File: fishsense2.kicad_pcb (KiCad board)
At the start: 2 copper layers, 71.1 x 73.7 mm, 20 parts, among them J1 Conn_02x10_Odd_Even, J2 Screw_Terminal_01x02, J3 Conn_01x02, J4 Conn_01x02, J5 Conn_01x02, J6 USB_C_Receptacle, J7 USB_C_Receptacle, J8 USB_C_Receptacle, K1 ADW11, U1 P783F-Q24-S5-S, U2 AD9951

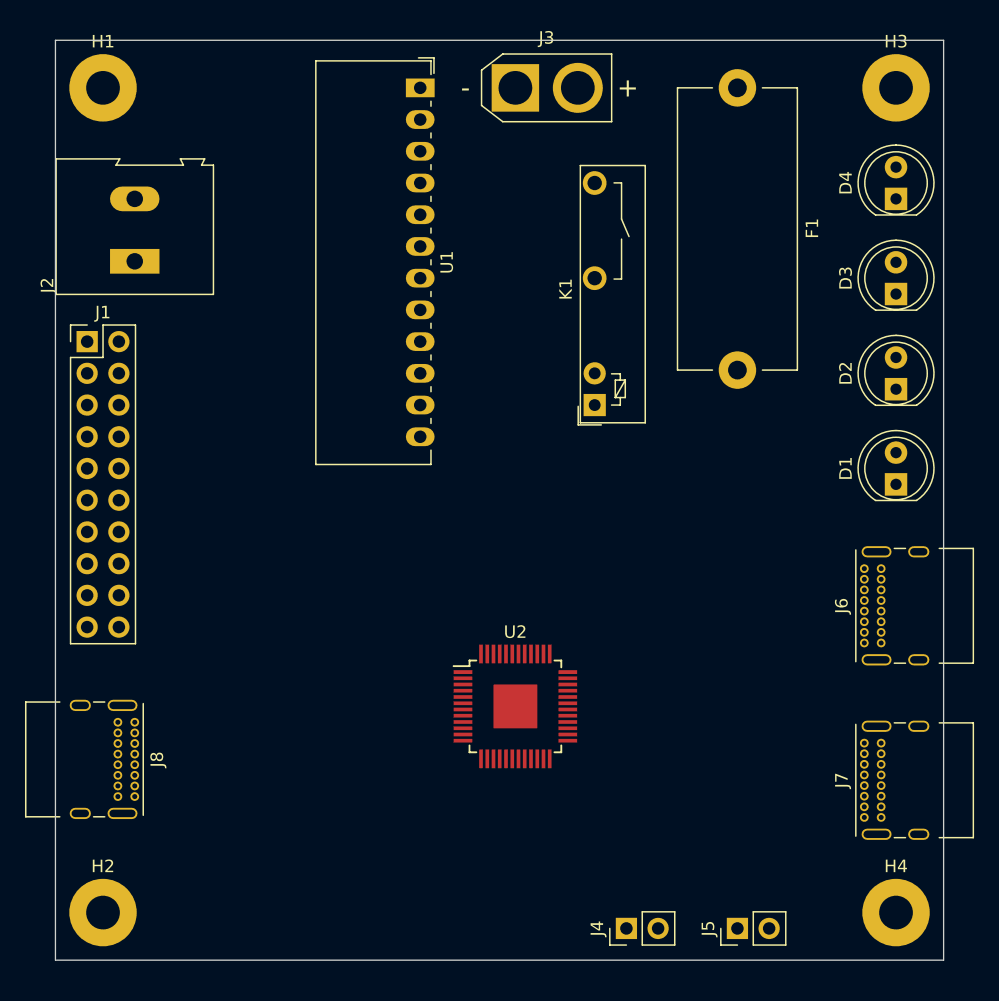
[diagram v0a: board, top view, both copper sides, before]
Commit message: Added symbols and footprints. More space for connectors on PCB.
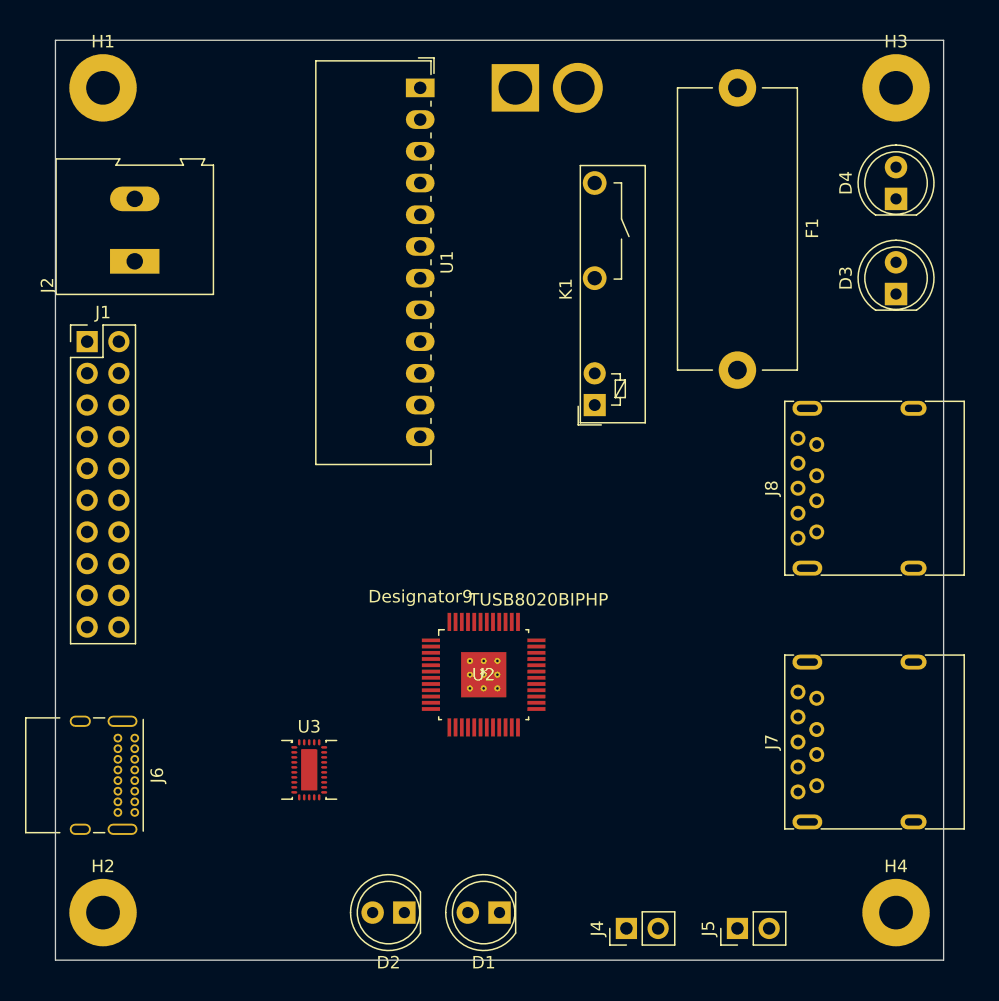
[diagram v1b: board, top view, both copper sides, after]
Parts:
- added U3: HD3SS3220, fishsense2:TI_VQFN_RNH, F.Cu at (148.6, 113.0)
- J3: moved to B.Cu
- J7, J8: value USB_C_Receptacle -> USB3_A; footprint Connector_USB:USB_C_Receptacle_GCT_USB4085 -> Connector_USB:USB3_A_Molex_48393-001
- U2: value AD9951 -> TUSB8020BIPHP; footprint Package_QFP:TQFP-48-1EP_7x7mm_P0.5mm_EP3.5x3.5mm -> fishsense2:TUSB8020BIPHP
- moved J6 58.9 mm to (134.6, 110.5), turned to 270 degrees
- moved D2 57.5 mm to (156.2, 124.5), turned to 180 degrees
- moved J8 56.7 mm to (189.2, 94.0), turned to 90 degrees
- moved D1 46.7 mm to (163.8, 124.5), turned to 180 degrees
- moved J7 4.58 mm to (189.2, 114.3)
- moved U2 3.59 mm to (162.6, 105.4)

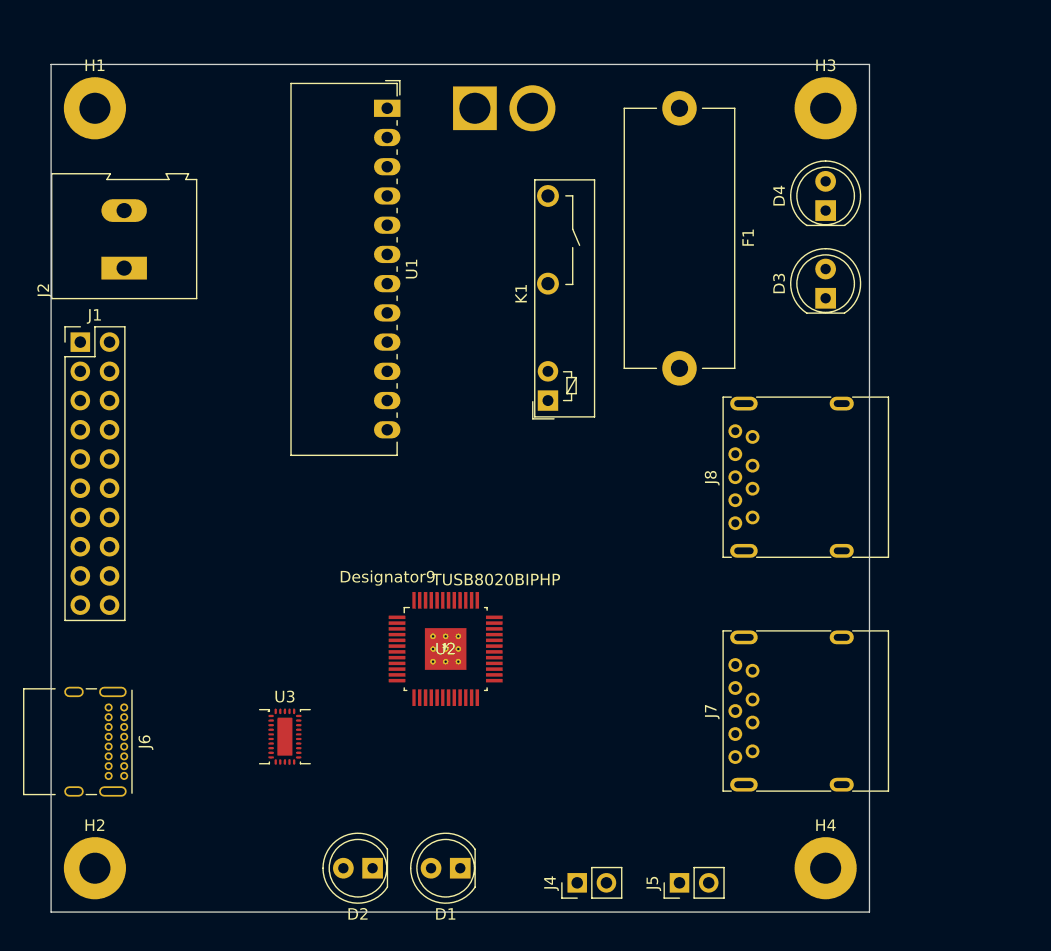
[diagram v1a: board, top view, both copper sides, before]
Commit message: Finished schematic. Added all footprints. Arranged components and routed differential signals.
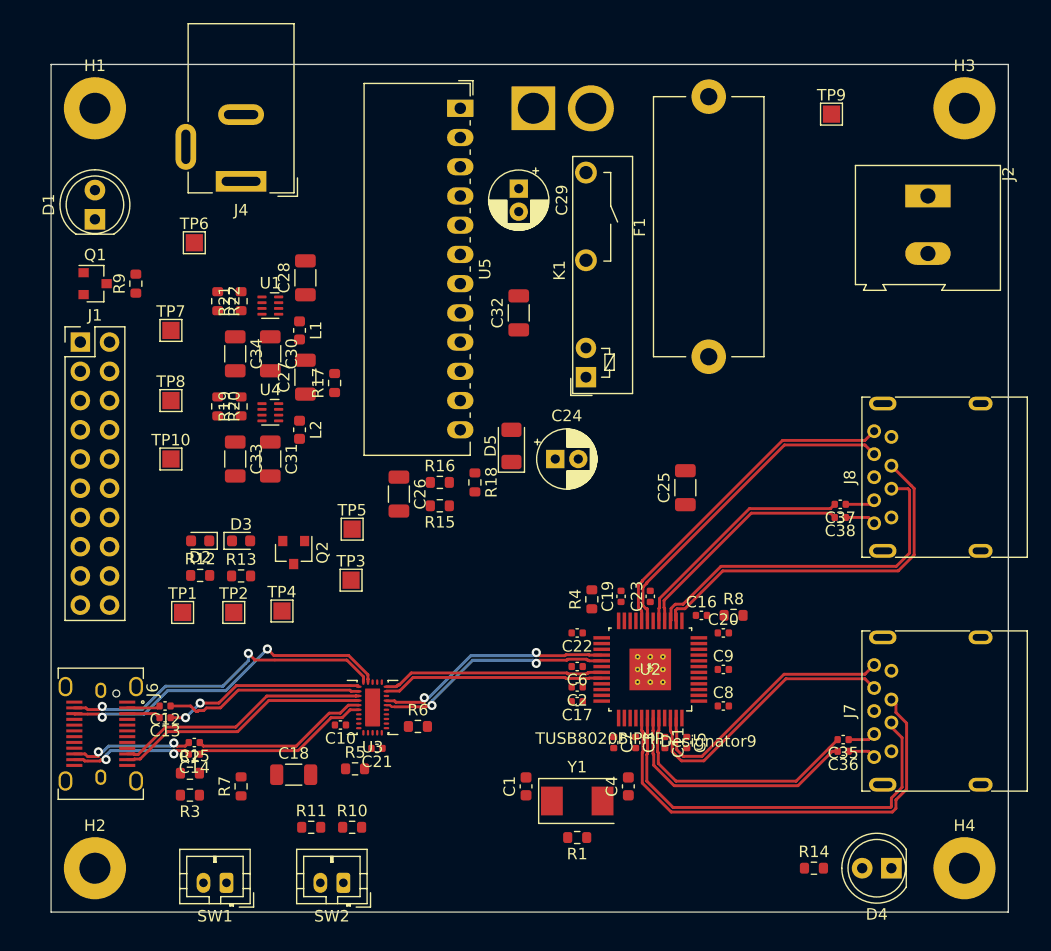
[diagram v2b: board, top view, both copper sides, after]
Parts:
- removed J5: Conn_01x02, Connector_PinHeader_2.54mm:PinHeader_1x02_P2.54mm_Vertical
- added C1: 18p, Capacitor_SMD:C_0603_1608Metric, F.Cu at (169.5, 117.3)
- added C10: 100n, Capacitor_SMD:C_0402_1005Metric, F.Cu at (153.4, 112.0)
- added C11: 0.1u, Capacitor_SMD:C_0402_1005Metric, F.Cu at (181.6, 113.5)
- added C12: 100n, Capacitor_SMD:C_0402_1005Metric, F.Cu at (138.2, 110.4)
- added C13: 100n, Capacitor_SMD:C_0402_1005Metric, F.Cu at (138.2, 111.4)
- added C14: 100n, Capacitor_SMD:C_0402_1005Metric, F.Cu at (140.7, 114.6)
- added C15: 100n, Capacitor_SMD:C_0402_1005Metric, F.Cu at (140.7, 113.5)
- added C16: 0.1u, Capacitor_SMD:C_0402_1005Metric, F.Cu at (184.8, 102.5)
- added C17: 0.1u, Capacitor_SMD:C_0402_1005Metric, F.Cu at (174.0, 110.0)
- added C18: 10u, Capacitor_SMD:C_1206_3216Metric, F.Cu at (149.4, 116.3)
- added C19: 0.1u, Capacitor_SMD:C_0402_1005Metric, F.Cu at (177.8, 100.8)
- added C2: 0.1u, Capacitor_SMD:C_0402_1005Metric, F.Cu at (174.0, 108.7)
- added C20: 0.1u, Capacitor_SMD:C_0402_1005Metric, F.Cu at (186.7, 104.0)
- added C21: 100n, Capacitor_SMD:C_0402_1005Metric, F.Cu at (156.6, 114.0)
- added C22: 0.1u, Capacitor_SMD:C_0402_1005Metric, F.Cu at (174.0, 104.0)
- added C23: 0.1u, Capacitor_SMD:C_0402_1005Metric, F.Cu at (180.3, 100.8)
- added C24: 100u, Capacitor_THT:CP_Radial_D5.0mm_P2.00mm, F.Cu at (172.1, 88.9)
- added C25: 1u, Capacitor_SMD:C_1206_3216Metric, F.Cu at (183.4, 91.4)
- added C26: 0.47u, Capacitor_SMD:C_1206_3216Metric, F.Cu at (158.5, 91.9)
- added C27: 4.7u, Capacitor_SMD:C_1206_3216Metric, F.Cu at (150.4, 81.8)
- added C28: 4.7u, Capacitor_SMD:C_1206_3216Metric, F.Cu at (150.4, 73.2)
- added C29: 100u, Capacitor_THT:CP_Radial_D5.0mm_P2.00mm, F.Cu at (168.9, 65.4)
- added C3: 0.1u, Capacitor_SMD:C_0402_1005Metric, F.Cu at (179.1, 113.5)
- added C30: 10u, Capacitor_SMD:C_1206_3216Metric, F.Cu at (147.3, 79.8)
- added C31: 10u, Capacitor_SMD:C_1206_3216Metric, F.Cu at (147.3, 88.9)
- added C32: 22u, Capacitor_SMD:C_1206_3216Metric, F.Cu at (168.9, 76.2)
- added C33: 10u, Capacitor_SMD:C_1206_3216Metric, F.Cu at (144.3, 88.9)
- added C34: 10u, Capacitor_SMD:C_1206_3216Metric, F.Cu at (144.3, 79.8)
- added C35: 0.1u, Capacitor_SMD:C_0402_1005Metric, F.Cu at (197.1, 113.3)
- added C36: 0.1u, Capacitor_SMD:C_0402_1005Metric, F.Cu at (197.1, 114.3)
- added C37: 0.1u, Capacitor_SMD:C_0402_1005Metric, F.Cu at (196.8, 92.8)
- added C38: 0.1u, Capacitor_SMD:C_0402_1005Metric, F.Cu at (196.8, 94.0)
- added C4: 18p, Capacitor_SMD:C_0603_1608Metric, F.Cu at (178.4, 117.3)
- added C5: 0.1u, Capacitor_SMD:C_0402_1005Metric, F.Cu at (183.5, 113.5)
- added C6: 0.1u, Capacitor_SMD:C_0402_1005Metric, F.Cu at (174.0, 106.9)
- added C7: 0.1u, Capacitor_SMD:C_0402_1005Metric, F.Cu at (177.2, 113.5)
- added C8: 0.1u, Capacitor_SMD:C_0402_1005Metric, F.Cu at (186.7, 110.4)
- added C9: 0.1u, Capacitor_SMD:C_0402_1005Metric, F.Cu at (186.7, 107.2)
- added D5: D_Schottky, Diode_SMD:D_1206_3216Metric, F.Cu at (168.3, 87.8)
- added L1: 0.47u, Inductor_SMD:L_0603_1608Metric, F.Cu at (149.9, 77.7)
- added L2: 0.47u, Inductor_SMD:L_0603_1608Metric, F.Cu at (149.9, 86.4)
- added Q1: Q_NMOS_DGS, Package_TO_SOT_SMD:SOT-23, F.Cu at (132.1, 73.7)
- added Q2: Q_NMOS_DSG, Package_TO_SOT_SMD:SOT-23, F.Cu at (149.4, 97.0)
- added R1: 1M, Resistor_SMD:R_0603_1608Metric, F.Cu at (174.0, 121.8)
- added R10: 10k, Resistor_SMD:R_0603_1608Metric, F.Cu at (154.4, 120.9)
- added R11: 5k6, Resistor_SMD:R_0603_1608Metric, F.Cu at (150.9, 120.9)
- added R12: 20k, Resistor_SMD:R_0603_1608Metric, F.Cu at (141.2, 99.0)
- added R13: 40k, Resistor_SMD:R_0603_1608Metric, F.Cu at (144.8, 99.1)
- added R14: 1k, Resistor_SMD:R_0603_1608Metric, F.Cu at (194.6, 124.5)
- added R15: 30k, Resistor_SMD:R_0603_1608Metric, F.Cu at (162.1, 93.0)
- added R16: 20k, Resistor_SMD:R_0603_1608Metric, F.Cu at (162.1, 90.9)
- added R17: 50k, Resistor_SMD:R_0603_1608Metric, F.Cu at (152.9, 82.3)
- added R18: 125k, Resistor_SMD:R_0603_1608Metric, F.Cu at (165.1, 90.9)
- added R19: 470k, Resistor_SMD:R_0603_1608Metric, F.Cu at (144.8, 84.3)
- added R2: 90k, Resistor_SMD:R_0603_1608Metric, F.Cu at (140.3, 116.2)
- added R20: 100k, Resistor_SMD:R_0603_1608Metric, F.Cu at (142.7, 84.3)
- added R21: 82k, Resistor_SMD:R_0603_1608Metric, F.Cu at (144.8, 75.2)
- added R22: 100k, Resistor_SMD:R_0603_1608Metric, F.Cu at (142.7, 75.2)
- added R3: 10k, Resistor_SMD:R_0603_1608Metric, F.Cu at (140.3, 118.1)
- added R4: 9k53, Resistor_SMD:R_0603_1608Metric, F.Cu at (175.3, 101.1)
- added R5: 200k, Resistor_SMD:R_0603_1608Metric, F.Cu at (154.7, 115.8)
- added R6: 4.7k, Resistor_SMD:R_0603_1608Metric, F.Cu at (160.1, 112.1)
- added R7: 900k, Resistor_SMD:R_0603_1608Metric, F.Cu at (144.8, 117.3)
- added R8: 1k, Resistor_SMD:R_0603_1608Metric, F.Cu at (187.6, 102.5)
- added R9: 220, Resistor_SMD:R_0603_1608Metric, F.Cu at (135.6, 73.7)
- added SW1: SW_Reed, Connector_JST:JST_PH_B2B-PH-K_1x02_P2.00mm_Vertical, F.Cu at (143.5, 125.7)
- added SW2: SW_Reed, Connector_JST:JST_PH_B2B-PH-K_1x02_P2.00mm_Vertical, F.Cu at (153.7, 125.7)
- added TP1: CC1, TestPoint:TestPoint_Pad_1.5x1.5mm, F.Cu at (139.7, 102.2)
- added TP10: 3.3v, TestPoint:TestPoint_Pad_1.5x1.5mm, F.Cu at (138.7, 88.9)
- added TP2: CC2, TestPoint:TestPoint_Pad_1.5x1.5mm, F.Cu at (144.1, 102.2)
- added TP3: Relay_Ctl, TestPoint:TestPoint_Pad_1.5x1.5mm, F.Cu at (154.3, 99.4)
- added TP4: Relay+, TestPoint:TestPoint_Pad_1.5x1.5mm, F.Cu at (148.3, 102.1)
- added TP5: Relay-, TestPoint:TestPoint_Pad_1.5x1.5mm, F.Cu at (154.4, 95.0)
- added TP6: 1.1v EN, TestPoint:TestPoint_Pad_1.5x1.5mm, F.Cu at (140.7, 70.1)
- added TP7: 3.3v EN, TestPoint:TestPoint_Pad_1.5x1.5mm, F.Cu at (138.7, 77.7)
- added TP8: 1.1v, TestPoint:TestPoint_Pad_1.5x1.5mm, F.Cu at (138.7, 83.8)
- added TP9: 5v, TestPoint:TestPoint_Pad_1.5x1.5mm, F.Cu at (196.1, 58.9)
- added U4: TPS62821DLC, Package_DFN_QFN:Texas_VSON-HR-8_1.5x2mm_P0.5mm, F.Cu at (147.3, 84.8)
- added U5: P783F-Q24-S5-S, Converter_DCDC:Converter_DCDC_RECOM_R5xxxPA_THT, F.Cu at (163.8, 58.4)
- added Y1: Crystal, Crystal:Crystal_SMD_0603-2Pin_6.0x3.5mm, F.Cu at (174.0, 118.6)
- D2, D3: value LED -> D; footprint LED_THT:LED_D5.0mm_FlatTop -> Diode_SMD:D_0603_1608Metric
- J2: value Screw_Terminal_01x02 -> BATT_OUT
- J3: value Conn_01x02 -> BATT_IN
- J4: value Conn_01x02 -> Barrel_Jack_Switch; footprint Connector_PinHeader_2.54mm:PinHeader_1x02_P2.54mm_Vertical -> Connector_BarrelJack:BarrelJack_Wuerth_6941xx301002
- J6: footprint Connector_USB:USB_C_Receptacle_GCT_USB4085 -> Connector_USB:USB_C_Receptacle_JAE_DX07S024WJ1R350
- K1: value ADW11 -> UMS05-1A80-75L
- U1: value P783F-Q24-S5-S -> TPS62821DLC; footprint Converter_DCDC:Converter_DCDC_RECOM_R5xxxPA_THT -> Package_DFN_QFN:Texas_VSON-HR-8_1.5x2mm_P0.5mm
- moved J2 70.1 mm to (204.5, 66.0), turned to 270 degrees
- moved J4 67.6 mm to (144.8, 64.8), turned to 180 degrees
- moved D1 64.7 mm to (132.1, 68.1), turned to 90 degrees
- moved D4 57.4 mm to (201.3, 124.5), turned to 180 degrees
- moved D3 55.0 mm to (144.8, 96.0), turned to 0 degrees
- moved D2 32.2 mm to (141.2, 96.0)
- moved F1 21.7 mm to (185.4, 80.0), turned to 90 degrees
- moved U1 19.9 mm to (147.3, 75.6), turned to 0 degrees
- moved U2 17.9 mm to (180.3, 107.2), turned to 180 degrees
- moved H3 12.1 mm to (207.6, 58.4)
- moved H4 12.1 mm to (207.6, 124.5)
- moved J7 12.1 mm to (201.3, 114.3)
- moved J8 12.1 mm to (201.3, 94.0)
- moved U3 8.03 mm to (156.2, 110.5), turned to 180 degrees
- moved J3 5.08 mm to (170.2, 58.4)
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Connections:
- net Net-(J6-PadA4) renamed /VBUS_UP
- D2 pad 1: Net-(D2-Pad1) -> /Power/RELAY+
- D2 pad 2: Net-(D2-Pad2) -> REED
- D3 pad 1: Net-(D3-Pad1) -> /Power/RELAY+
- D3 pad 2: Net-(D3-Pad2) -> +5V
- D4 pad 1: Net-(D4-Pad1) -> GND
- F1 pad 1: Net-(F1-Pad1) -> +15V
- H1 pad 1: Net-(H1-Pad1) -> GND
- H2 pad 1: Net-(H2-Pad1) -> GND
- H3 pad 1: Net-(H3-Pad1) -> GND
- H4 pad 1: Net-(H4-Pad1) -> GND
- J1 pad 10: Net-(J1-Pad10) -> RELAY_CTL
- J1 pad 16: Net-(J1-Pad16) -> GND
- J1 pad 18: Net-(J1-Pad18) -> GND
- J1 pad 19: Net-(J1-Pad19) -> GND
- J1 pad 20: Net-(J1-Pad20) -> GND
- J1 pad 8: Net-(J1-Pad8) -> REED
- J2 pad 1: Net-(J2-Pad1) -> GND
- J2 pad 2: Net-(J2-Pad2) -> /Power/BATT_SWITCHED
- J3 pad 1: Net-(J3-Pad1) -> GND
- J3 pad 2: Net-(J3-Pad2) -> Net-(F1-Pad2)
- J4 pad 1: Net-(J4-Pad1) -> +5V
- J4 pad 2: Net-(J4-Pad2) -> GND
- J6 pad A1: Net-(J6-PadA1) -> GND
- J6 pad A12: Net-(J6-PadA1) -> GND
- J6 pad A5: Net-(J6-PadA5) -> /CC1
- J6 pad A6: Net-(J6-PadA6) -> /D_UP_P
- J6 pad A7: Net-(J6-PadA7) -> /D_UP_N
- J6 pad B1: Net-(J6-PadA1) -> GND
- J6 pad B12: Net-(J6-PadA1) -> GND
- J6 pad B5: Net-(J6-PadB5) -> /CC2
- J6 pad B6: Net-(J6-PadB6) -> /D_UP_P
- J6 pad B7: Net-(J6-PadB7) -> /D_UP_N
- J6 pad S1: Net-(J6-PadS1) -> GND
- J7 pad 1: Net-(J7-Pad1) -> +5V
- J7 pad 10: Net-(J7-Pad10) -> GND
- J7 pad 2: Net-(J7-Pad2) -> /D_DN1_N
- J7 pad 3: Net-(J7-Pad3) -> /D_DN1_P
- J7 pad 4: Net-(J7-Pad4) -> GND
- J7 pad 5: Net-(J7-Pad5) -> /RX_DN1_N
- J7 pad 6: Net-(J7-Pad6) -> /RX_DN1_P
- J7 pad 7: Net-(J7-Pad7) -> GND
- J7 pad 8: Net-(J7-Pad8) -> /TX_DN1_F_N
- J7 pad 9: Net-(J7-Pad9) -> /TX_DN1_F_P
- J8 pad 1: Net-(J8-Pad1) -> +5V
- J8 pad 10: Net-(J8-Pad10) -> GND
- J8 pad 2: Net-(J8-Pad2) -> /D_DN2_N
- J8 pad 3: Net-(J8-Pad3) -> /D_DN2_P
- J8 pad 4: Net-(J8-Pad4) -> GND
- J8 pad 5: Net-(J8-Pad5) -> /RX_DN2_N
- J8 pad 6: Net-(J8-Pad6) -> /RX_DN2_P
- J8 pad 7: Net-(J8-Pad7) -> GND
- J8 pad 8: Net-(J8-Pad8) -> /TX_DN2_F_N
- J8 pad 9: Net-(J8-Pad9) -> /TX_DN2_F_P
- K1 pad 1: Net-(K1-Pad1) -> /Power/RELAY-
- K1 pad 2: (no net) -> /Power/RELAY+
- K1 pad 3: Net-(K1-Pad3) -> /Power/BATT_SWITCHED
- K1 pad 4: (no net) -> +15V
- U1 pad 3: Net-(U1-Pad3) -> GND
- U1 pad 5: Net-(U1-Pad5) -> GND
- U1 pad 7: Net-(U1-Pad7) -> +5V
- U2 pad 1: Net-(U2-Pad1) -> +5V
- U2 pad 12: Net-(U2-Pad12) -> +5V
- U2 pad 13: Net-(U2-Pad13) -> +3V3
- U2 pad 14: Net-(U2-Pad14) -> /D_DN2_P
- U2 pad 15: Net-(U2-Pad15) -> /D_DN2_N
- U2 pad 16: Net-(U2-Pad16) -> /TX_DN2_P
- U2 pad 17: Net-(U2-Pad17) -> /TX_DN2_N
- U2 pad 18: Net-(U2-Pad18) -> +5V
- U2 pad 19: Net-(U2-Pad19) -> /RX_DN2_P
- U2 pad 20: Net-(U2-Pad20) -> /RX_DN2_N
- U2 pad 23: Net-(U2-Pad23) -> +3V3
- U2 pad 25: Net-(U2-Pad25) -> +3V3
- U2 pad 26: Net-(U2-Pad26) -> /D_UP_P
- U2 pad 27: Net-(U2-Pad27) -> /D_UP_N
- U2 pad 28: Net-(U2-Pad28) -> /TX_N
- U2 pad 29: Net-(U2-Pad29) -> /TX_P
- U2 pad 30: Net-(U2-Pad30) -> +5V
- U2 pad 31: Net-(U2-Pad31) -> /RX_N
- U2 pad 32: Net-(U2-Pad32) -> /RX_P
- U2 pad 33: Net-(U2-Pad33) -> +3V3
- U2 pad 34: Net-(U2-Pad34) -> +5V
- U2 pad 37: Net-(U2-Pad37) -> +3V3
- U2 pad 38: Net-(U2-Pad38) -> /XI
- U2 pad 39: Net-(U2-Pad39) -> /XO
- U2 pad 40: Net-(U2-Pad40) -> +3V3
- U2 pad 41: Net-(U2-Pad41) -> /D_DN1_P
- U2 pad 42: Net-(U2-Pad42) -> /D_DN1_N
- U2 pad 43: Net-(U2-Pad43) -> /TX_DN1_P
- U2 pad 44: Net-(U2-Pad44) -> /TX_DN1_N
- U2 pad 45: Net-(U2-Pad45) -> +5V
- U2 pad 46: Net-(U2-Pad46) -> /RX_DN1_P
- U2 pad 47: Net-(U2-Pad47) -> /RX_DN1_N
- U2 pad 48: Net-(U2-Pad48) -> +3V3
- U2 pad 49: Net-(U2-Pad49) -> GND
- U2 pad 7: Net-(U2-Pad7) -> +3V3
- U3 pad 1: Net-(U3-Pad1) -> /CC2
- U3 pad 10: Net-(U3-Pad10) -> /RX_N
- U3 pad 12: Net-(U3-Pad12) -> GND
- U3 pad 13: Net-(U3-Pad13) -> GND
- U3 pad 14: Net-(U3-Pad14) -> /RX1_N
- U3 pad 15: Net-(U3-Pad15) -> /RX1_P
- U3 pad 16: Net-(U3-Pad16) -> /TX1_F_N
- U3 pad 17: Net-(U3-Pad17) -> /TX1_F_P
- U3 pad 18: Net-(U3-Pad18) -> /RX2_N
- U3 pad 19: Net-(U3-Pad19) -> /RX2_P
- U3 pad 2: Net-(U3-Pad2) -> /CC1
- U3 pad 20: Net-(U3-Pad20) -> /TX2_F_N
- U3 pad 21: Net-(U3-Pad21) -> /TX2_F_P
- U3 pad 28: Net-(U3-Pad28) -> GND
- U3 pad 29: Net-(U3-Pad29) -> GND
- U3 pad 30: Net-(U3-Pad30) -> +5V
- U3 pad 5: (no net) -> Net-(R7-Pad1)
- U3 pad 6: Net-(U3-Pad6) -> /TX_P
- U3 pad 7: Net-(U3-Pad7) -> /TX_N
- U3 pad 8: Net-(U3-Pad8) -> +3V3
- U3 pad 9: Net-(U3-Pad9) -> /RX_P
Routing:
- net /D_DN1_P: track 0.00 -> 39.3 mm
- net /D_DN1_N: track 0.00 -> 35.8 mm
- net /D_DN2_P: track 0.00 -> 32.2 mm
- net /D_DN2_N: track 0.00 -> 30.9 mm
- net /RX1_N: track 0.00 -> 29.7 mm, vias 0 -> 2
- net /RX_DN2_N: track 0.00 -> 29.3 mm
- net /RX1_P: track 0.00 -> 29.2 mm, vias 0 -> 2
- net /RX_DN2_P: track 0.00 -> 28.7 mm
- net /RX_DN1_P: track 0.00 -> 24.1 mm
- net /RX_DN1_N: track 0.00 -> 23.5 mm
- net /RX2_P: track 0.00 -> 22.3 mm
- net /RX2_N: track 0.00 -> 22.3 mm
- net /TX_DN1_P: track 0.00 -> 22.1 mm
- net /TX_DN1_N: track 0.00 -> 21.7 mm
- net /TX_P: track 0.00 -> 21.0 mm, vias 0 -> 2
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- added copper zone on In1.Cu, net GND
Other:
- board size 71.1 x 73.7 mm -> 83.2 x 73.7 mm
- copper layers 2 -> 4
- net class Default: clearance 0.2 -> 0.127; trace_width 0.25 -> 0.2
- net class USB added: clearance 0.127, trace_width 0.25, via_dia 0.8, via_drill 0.4
- rule trace_clearance: 0.2 -> 0.127
- rule trace_min: 0.2 -> 0.127
